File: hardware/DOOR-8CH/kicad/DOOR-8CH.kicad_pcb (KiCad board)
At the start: 4 copper layers, 260 x 160 mm, 230 parts, among them J1 FUSED_12V_CH1, J10 ACTUATOR_CH2, J11 ACTUATOR_CH3, J12 ACTUATOR_CH4, J13 ACTUATOR_CH5, J14 ACTUATOR_CH6, J15 ACTUATOR_CH7, J16 ACTUATOR_CH8, J2 FUSED_12V_CH2, J201 REED_A_OPEN_3V3_SIG_GND, J202 REED_A_CLOSED_3V3_SIG_GND, J203 REED_A_IN_PLACE_3V3_SIG_GND, J204 REED_B_OPEN_3V3_SIG_GND, J205 REED_B_CLOSED_3V3_SIG_GND, J206 REED_B_IN_PLACE_3V3_SIG_GND, J211 CAP_CS1_GND, J212 CAP_CS2_GND, J213 CAP_CS3_GND, J214 CAP_CS4_GND, J215 CAP_CS5_GND, J216 CAP_CS6_GND, J217 CAP_CS7_GND, J218 CAP_CS8_GND, J220 SWD_S1_3V3_DIO_CLK_NRST_GND, J230 LOGIC_12V_GND, J240 CANH_CANL_GND_SHIELD, J3 FUSED_12V_CH3, J4 FUSED_12V_CH4, J5 FUSED_12V_CH5, J6 FUSED_12V_CH6, J7 FUSED_12V_CH7, J8 FUSED_12V_CH8, J9 ACTUATOR_CH1, U1 VNH5019A-E, U2 VNH5019A-E, U230 AMS1117-3V3, U250 25LC256_SOIC8_CARRIER_ID, U3 VNH5019A-E, U4 VNH5019A-E, U5 VNH5019A-E, U6 VNH5019A-E, U7 VNH5019A-E, U8 VNH5019A-E

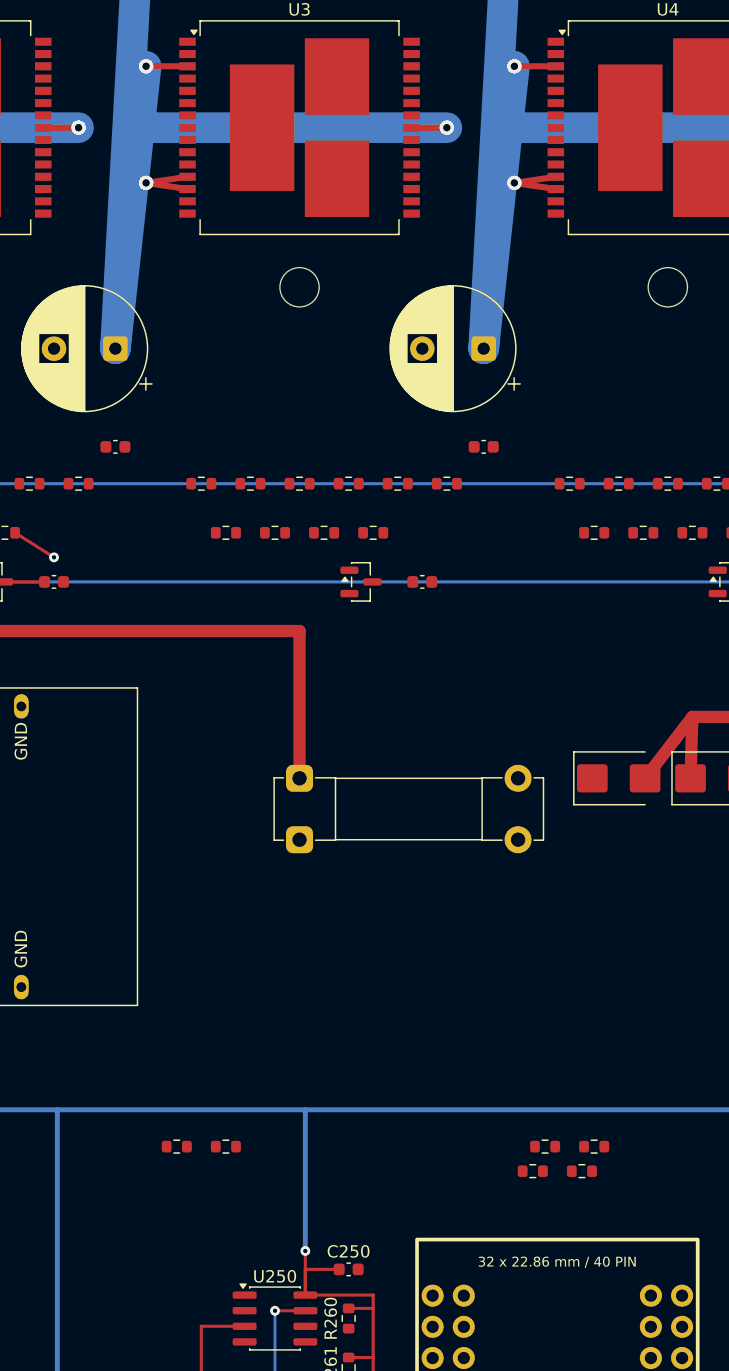
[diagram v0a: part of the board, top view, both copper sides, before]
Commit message: Route channel 3 controls and current measurement
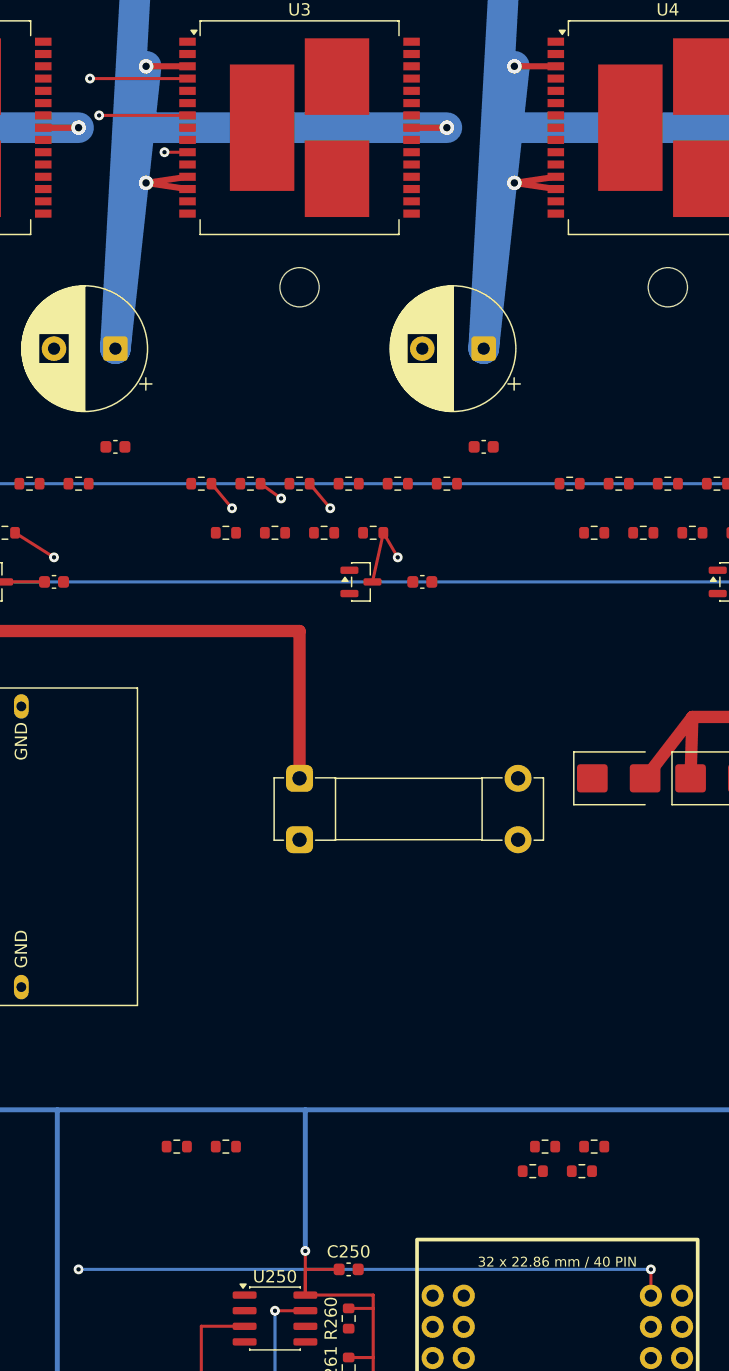
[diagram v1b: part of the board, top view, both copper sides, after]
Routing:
- net CH3_CURRENT_ADC: track 0.00 -> 139.2 mm, vias 0 -> 3
- net CH3_PWM: track 0.00 -> 72.6 mm, vias 0 -> 2
- net CH3_INA: track 0.00 -> 65.1 mm, vias 0 -> 2
- net CH3_INB: track 0.00 -> 41.6 mm, vias 0 -> 2
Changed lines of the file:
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@@
+	)
+	(segment
+		(start 82.5 65.2)
+		(end 80.83 64)
+		(width 0.25)
+		(layer "F.Cu")
+		(net "CH3_INB")
+	)
+	(segment
+		(start 74.88 37)
+		(end 73 37)
+		(width 0.25)
+		(layer "F.Cu")
+		(net "CH3_INB")
+	)
+	(via
+		(at 73 37)
+		(size 0.8)
+		(drill 0.35)
+		(layers "F.Cu" "B.Cu")
+		(net "CH3_INB")
+	)
+	(via
+		(at 82.5 65.2)
+		(size 0.8)
+		(drill 0.35)
+		(layers "F.Cu" "B.Cu")
+		(net "CH3_INB")
+	)
+	(segment
+		(start 73 37)
+		(end 73 65.2)
+		(width 0.25)
+		(layer "In2.Cu")
+		(net "CH3_INB")
+	)
+	(segment
+		(start 73 65.2)
+		(end 82.5 65.2)
+		(width 0.25)
+		(layer "In2.Cu")
+		(net "CH3_INB")
 	)
 	(segment
@@
 	)
 	(segment
+		(start 90.83 68)
+		(end 89.94 72)
+		(width 0.25)
+		(layer "F.Cu")
+		(net "CH3_CURRENT_ADC")
+	)
+	(segment
+		(start 90.83 68)
+		(end 92 70)
+		(width 0.25)
+		(layer "F.Cu")
+		(net "CH3_CURRENT_ADC")
+	)
+	(segment
+		(start 112.62 128)
+		(end 112.62 130.139999)
+		(width 0.25)
+		(layer "F.Cu")
+		(net "CH3_CURRENT_ADC")
+	)
+	(via
+		(at 92 70)
+		(size 0.8)
+		(drill 0.35)
+		(layers "F.Cu" "B.Cu")
+		(net "CH3_CURRENT_ADC")
+	)
+	(via
+		(at 112.62 128)
+		(size 0.8)
+		(drill 0.35)
+		(layers "F.Cu" "B.Cu")
+		(net "CH3_CURRENT_ADC")
+	)
+	(via
+		(at 66 128)
+		(size 0.8)
+		(drill 0.35)
+		(layers "F.Cu" "B.Cu")
+		(net "CH3_CURRENT_ADC")
+	)
+	(segment
+		(start 66 128)
+		(end 112.62 128)
+		(width 0.25)
+		(layer "B.Cu")
+		(net "CH3_CURRENT_ADC")
+	)
+	(segment
+		(start 92 70)
+		(end 92 105)
+		(width 0.25)
+		(layer "In1.Cu")
+		(net "CH3_CURRENT_ADC")
+	)
+	(segment
+		(start 66 105)
+		(end 66 128)
+		(width 0.25)
+		(layer "In1.Cu")
+		(net "CH3_CURRENT_ADC")
+	)
+	(segment
+		(start 92 105)
+		(end 66 105)
+		(width 0.25)
+		(layer "In1.Cu")
+		(net "CH3_CURRENT_ADC")
+	)
+	(segment
+		(start 78.5 66)
+		(end 76.83 64)
+		(width 0.25)
+		(layer "F.Cu")
+		(net "CH3_INA")
+	)
+	(segment
+		(start 74.88 31)
+		(end 66.93 31)
+		(width 0.25)
+		(layer "F.Cu")
+		(net "CH3_INA")
+	)
+	(via
+		(at 66.93 31)
+		(size 0.8)
+		(drill 0.35)
+		(layers "F.Cu" "B.Cu")
+		(net "CH3_INA")
+	)
+	(via
+		(at 78.5 66)
+		(size 0.8)
+		(drill 0.35)
+		(layers "F.Cu" "B.Cu")
+		(net "CH3_INA")
+	)
+	(segment
+		(start 66.93 70)
+		(end 78.5 70)
+		(width 0.25)
+		(layer "In2.Cu")
+		(net "CH3_INA")
+	)
+	(segment
+		(start 78.5 70)
+		(end 78.5 66)
+		(width 0.25)
+		(layer "In2.Cu")
+		(net "CH3_INA")
+	)
+	(segment
+		(start 66.93 31)
+		(end 66.93 70)
+		(width 0.25)
+		(layer "In2.Cu")
+		(net "CH3_INA")
+	)
+	(segment
+		(start 74.88 34)
+		(end 67.675 34)
+		(width 0.25)
+		(layer "F.Cu")
+		(net "CH3_PWM")
+	)
+	(segment
+		(start 86.5 66)
+		(end 84.83 64)
+		(width 0.25)
+		(layer "F.Cu")
+		(net "CH3_PWM")
+	)
+	(via
+		(at 86.5 66)
+		(size 0.8)
+		(drill 0.35)
+		(layers "F.Cu" "B.Cu")
+		(net "CH3_PWM")
+	)
+	(via
+		(at 67.675 34)
+		(size 0.8)
+		(drill 0.35)
+		(layers "F.Cu" "B.Cu")
+		(net "CH3_PWM")
+	)
+	(segment
+		(start 67.675 72)
+		(end 86.5 72)
+		(width 0.25)
+		(layer "In1.Cu")
+		(net "CH3_PWM")
+	)
+	(segment
+		(start 67.675 34)
+		(end 67.675 72)
+		(width 0.25)
+		(layer "In1.Cu")
+		(net "CH3_PWM")
+	)
+	(segment
+		(start 86.5 72)
+		(end 86.5 66)
+		(width 0.25)
+		(layer "In1.Cu")
+		(net "CH3_PWM")
+	)
+	(segment

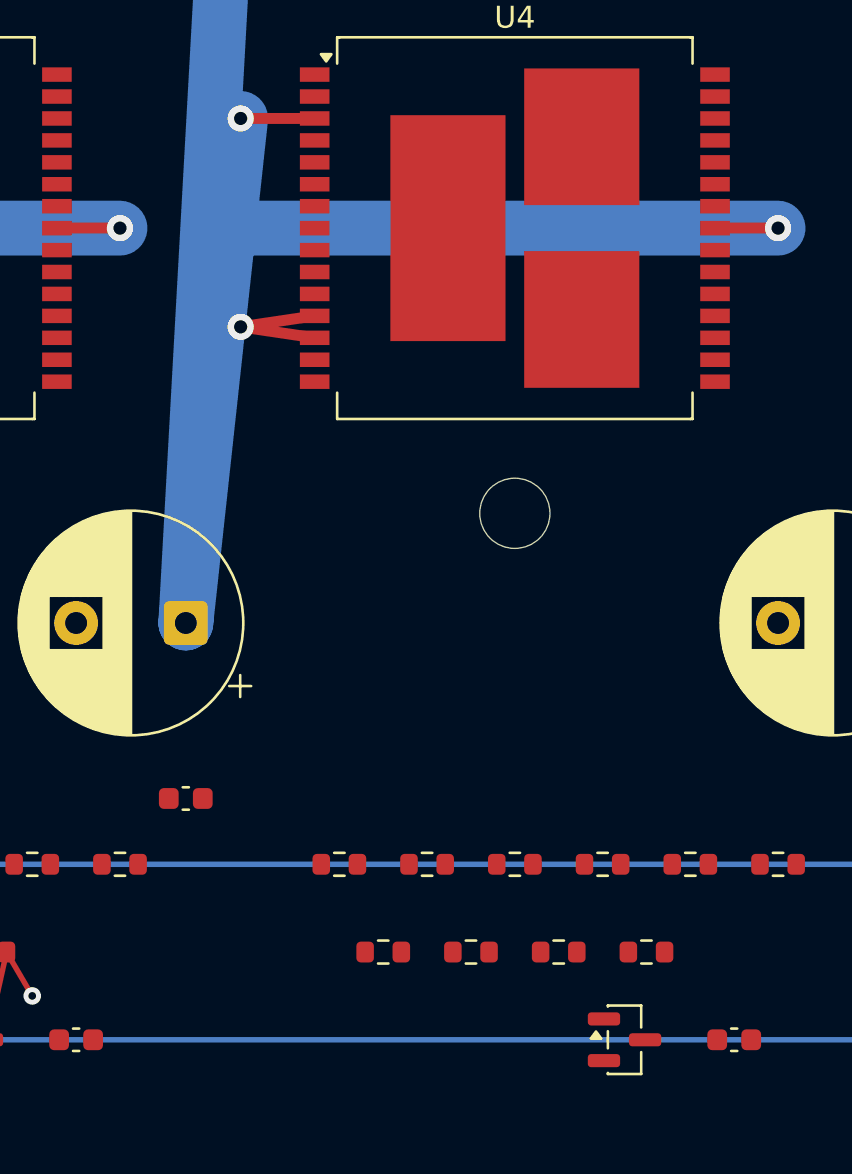
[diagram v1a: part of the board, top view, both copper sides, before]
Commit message: Route channel 4 controls and local current filter
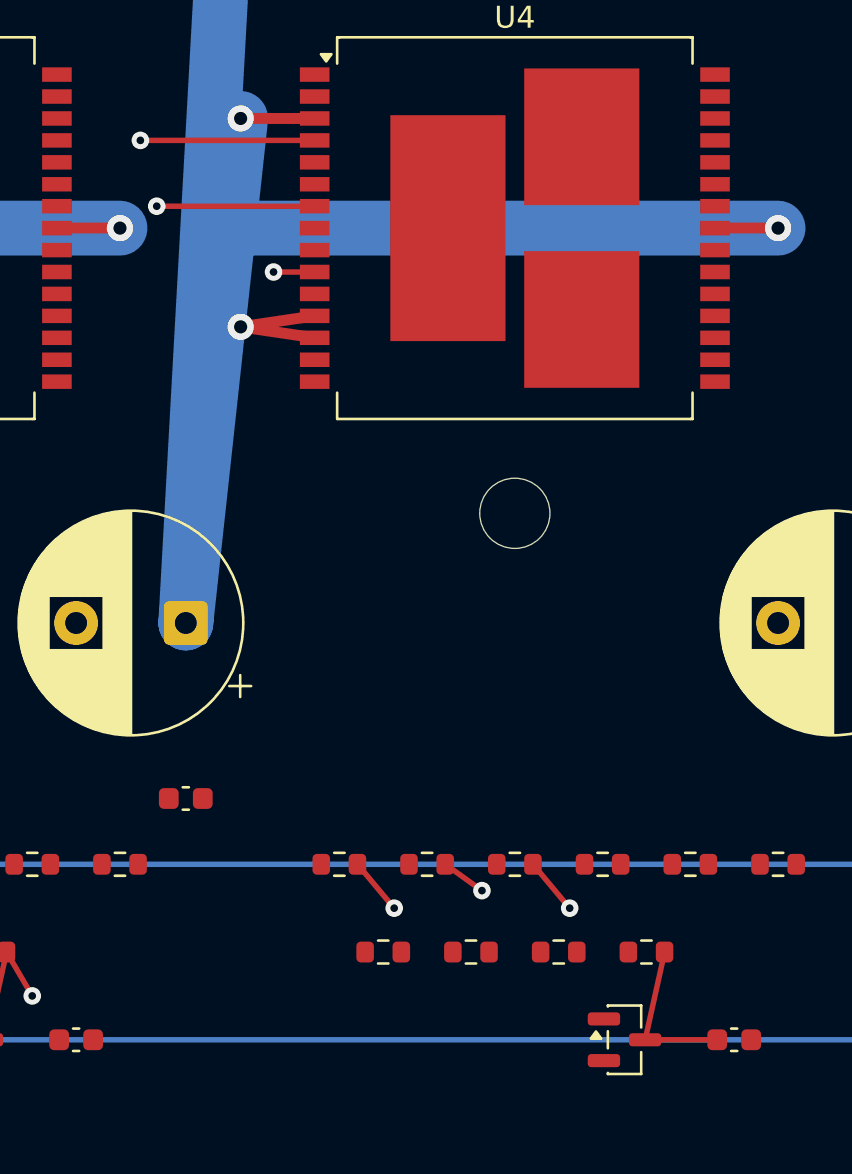
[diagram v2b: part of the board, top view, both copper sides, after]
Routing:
- net CH4_PWM: track 0.00 -> 72.6 mm, vias 0 -> 2
- net CH4_INA: track 0.00 -> 65.1 mm, vias 0 -> 2
- net CH4_INB: track 0.00 -> 41.6 mm, vias 0 -> 2
- net CH4_CURRENT_ADC: track 0.00 -> 7.39 mm
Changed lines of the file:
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@@
+	)
+	(segment
+		(start 120.83 68)
+		(end 119.94 72)
+		(width 0.25)
+		(layer "F.Cu")
+		(net "CH4_CURRENT_ADC")
+	)
+	(segment
+		(start 119.94 72)
+		(end 123.23 72)
+		(width 0.25)
+		(layer "F.Cu")
+		(net "CH4_CURRENT_ADC")
 	)
 	(segment
@@
 	)
 	(segment
+		(start 104.88 37)
+		(end 103 37)
+		(width 0.25)
+		(layer "F.Cu")
+		(net "CH4_INB")
+	)
+	(segment
+		(start 112.5 65.2)
+		(end 110.83 64)
+		(width 0.25)
+		(layer "F.Cu")
+		(net "CH4_INB")
+	)
+	(via
+		(at 112.5 65.2)
+		(size 0.8)
+		(drill 0.35)
+		(layers "F.Cu" "B.Cu")
+		(net "CH4_INB")
+	)
+	(via
+		(at 103 37)
+		(size 0.8)
+		(drill 0.35)
+		(layers "F.Cu" "B.Cu")
+		(net "CH4_INB")
+	)
+	(segment
+		(start 103 37)
+		(end 103 65.2)
+		(width 0.25)
+		(layer "In2.Cu")
+		(net "CH4_INB")
+	)
+	(segment
+		(start 103 65.2)
+		(end 112.5 65.2)
+		(width 0.25)
+		(layer "In2.Cu")
+		(net "CH4_INB")
+	)
+	(segment
 		(start 55.18 68)
 		(end 55.18 69)
@@
 	)
 	(segment
+		(start 116.5 66)
+		(end 114.83 64)
+		(width 0.25)
+		(layer "F.Cu")
+		(net "CH4_PWM")
+	)
+	(segment
+		(start 104.88 34)
+		(end 97.675 34)
+		(width 0.25)
+		(layer "F.Cu")
+		(net "CH4_PWM")
+	)
+	(via
+		(at 97.675 34)
+		(size 0.8)
+		(drill 0.35)
+		(layers "F.Cu" "B.Cu")
+		(net "CH4_PWM")
+	)
+	(via
+		(at 116.5 66)
+		(size 0.8)
+		(drill 0.35)
+		(layers "F.Cu" "B.Cu")
+		(net "CH4_PWM")
+	)
+	(segment
+		(start 97.675 34)
+		(end 97.675 72)
+		(width 0.25)
+		(layer "In1.Cu")
+		(net "CH4_PWM")
+	)
+	(segment
+		(start 97.675 72)
+		(end 116.5 72)
+		(width 0.25)
+		(layer "In1.Cu")
+		(net "CH4_PWM")
+	)
+	(segment
+		(start 116.5 72)
+		(end 116.5 66)
+		(width 0.25)
+		(layer "In1.Cu")
+		(net "CH4_PWM")
+	)
+	(segment
+		(start 104.88 31)
+		(end 96.93 31)
+		(width 0.25)
+		(layer "F.Cu")
+		(net "CH4_INA")
+	)
+	(segment
+		(start 108.5 66)
+		(end 106.83 64)
+		(width 0.25)
+		(layer "F.Cu")
+		(net "CH4_INA")
+	)
+	(via
+		(at 96.93 31)
+		(size 0.8)
+		(drill 0.35)
+		(layers "F.Cu" "B.Cu")
+		(net "CH4_INA")
+	)
+	(via
+		(at 108.5 66)
+		(size 0.8)
+		(drill 0.35)
+		(layers "F.Cu" "B.Cu")
+		(net "CH4_INA")
+	)
+	(segment
+		(start 96.93 70)
+		(end 108.5 70)
+		(width 0.25)
+		(layer "In2.Cu")
+		(net "CH4_INA")
+	)
+	(segment
+		(start 108.5 70)
+		(end 108.5 66)
+		(width 0.25)
+		(layer "In2.Cu")
+		(net "CH4_INA")
+	)
+	(segment
+		(start 96.93 31)
+		(end 96.93 70)
+		(width 0.25)
+		(layer "In2.Cu")
+		(net "CH4_INA")
+	)
+	(segment

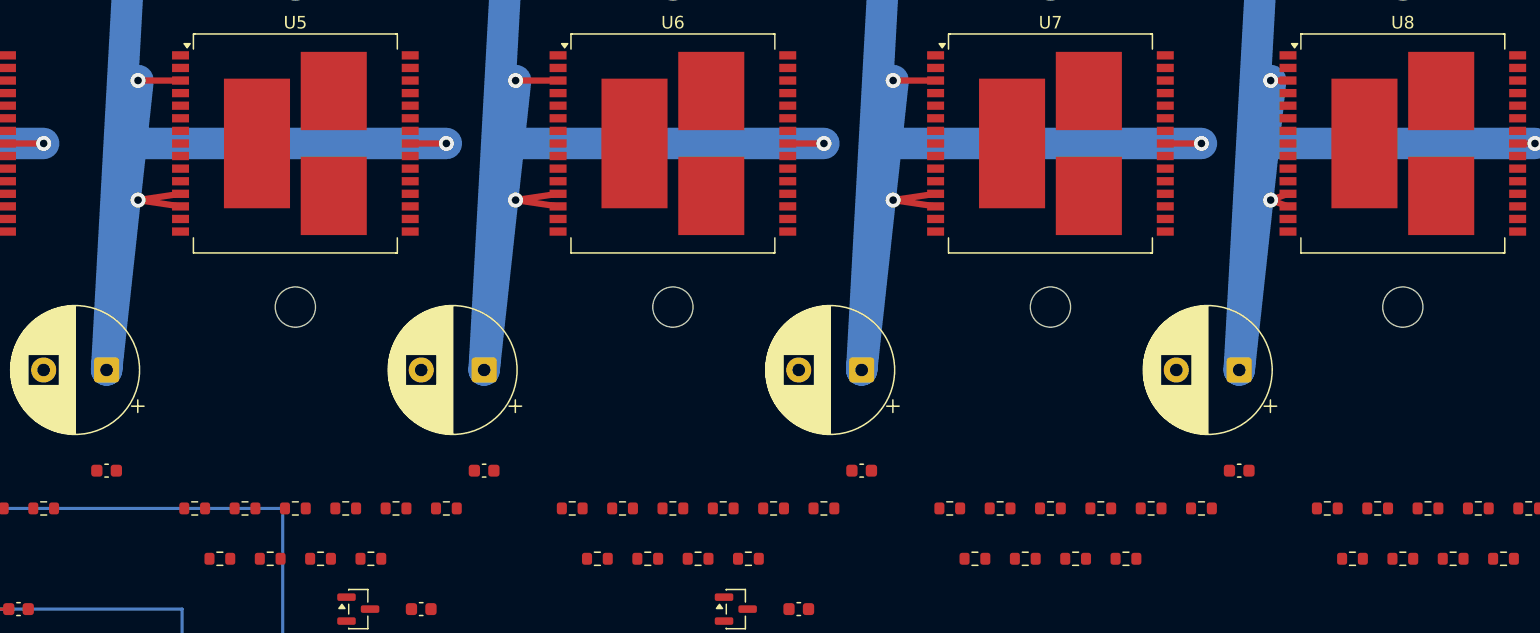
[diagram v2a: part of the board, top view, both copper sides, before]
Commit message: Route channels 5-8 VNH control inputs
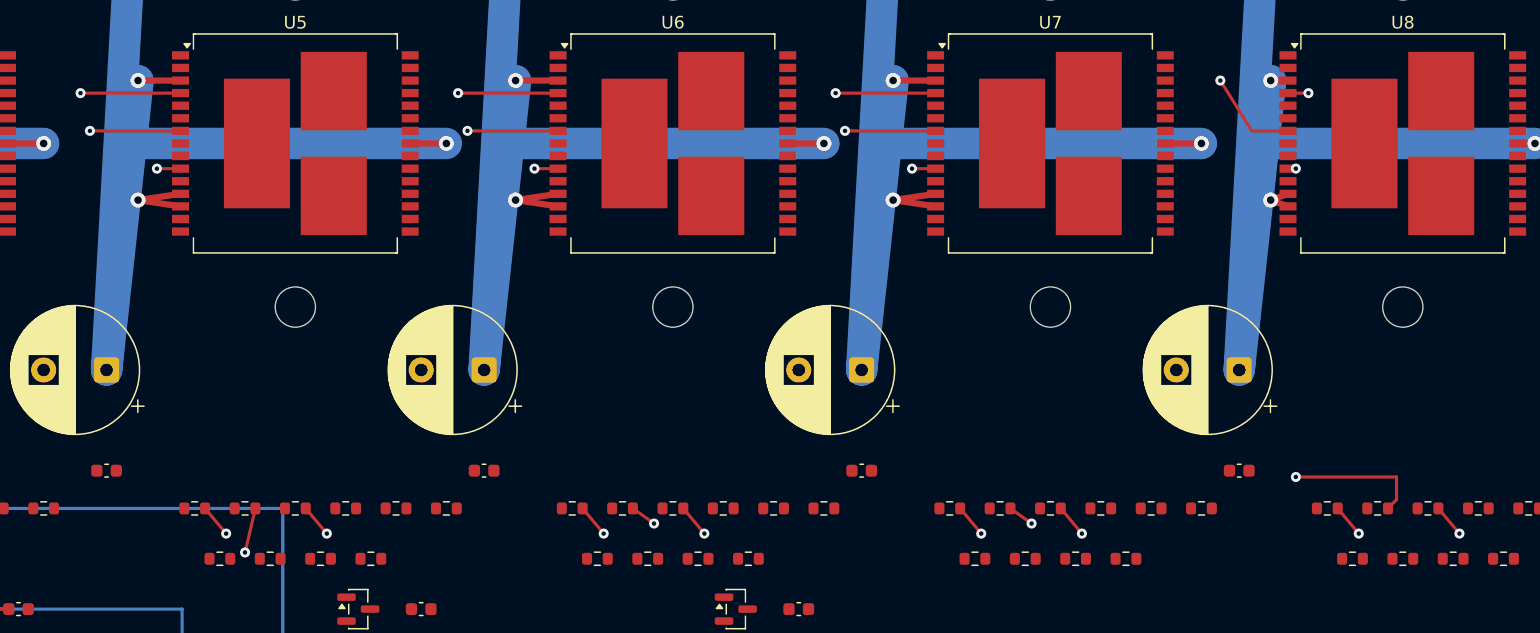
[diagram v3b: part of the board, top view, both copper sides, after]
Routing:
- net CH8_PWM: track 0.00 -> 88.2 mm, vias 0 -> 2
- net CH7_PWM: track 0.00 -> 72.6 mm, vias 0 -> 2
- net CH6_PWM: track 0.00 -> 72.6 mm, vias 0 -> 2
- net CH5_PWM: track 0.00 -> 72.6 mm, vias 0 -> 2
- net CH7_INA: track 0.00 -> 65.1 mm, vias 0 -> 2
- net CH6_INA: track 0.00 -> 65.1 mm, vias 0 -> 2
- net CH5_INA: track 0.00 -> 65.1 mm, vias 0 -> 2
- net CH8_INA: track 0.00 -> 51.2 mm, vias 0 -> 2
- net CH5_INB: track 0.00 -> 43.0 mm, vias 0 -> 2
- net CH7_INB: track 0.00 -> 41.6 mm, vias 0 -> 2
- net CH6_INB: track 0.00 -> 41.6 mm, vias 0 -> 2
- net CH8_INB: track 0.00 -> 35.9 mm, vias 0 -> 2

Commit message: Route channels 5-8 current filters
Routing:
- net CH7_CURRENT_ADC: track 0.00 -> 26.7 mm
- net CH8_CURRENT_ADC: track 0.00 -> 11.3 mm
- net CH6_CURRENT_ADC: track 0.00 -> 7.38 mm
- net CH5_CURRENT_ADC: track 0.00 -> 7.38 mm
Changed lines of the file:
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@@
+	)
+	(segment
+		(start 242.825 68)
+		(end 240.9375 76)
+		(width 0.25)
+		(layer "F.Cu")
+		(net "CH8_CURRENT_ADC")
+	)
+	(segment
+		(start 240.9375 76)
+		(end 243.225 78)
+		(width 0.25)
+		(layer "F.Cu")
+		(net "CH8_CURRENT_ADC")
 	)
 	(segment
@@
 		(layer "In1.Cu")
 		(net "CH7_PWM")
+	)
+	(segment
+		(start 212 84)
+		(end 205.5 84)
+		(width 0.25)
+		(layer "F.Cu")
+		(net "CH7_CURRENT_ADC")
+	)
+	(segment
+		(start 212 80)
+		(end 212 84)
+		(width 0.25)
+		(layer "F.Cu")
+		(net "CH7_CURRENT_ADC")
+	)
+	(segment
+		(start 210.9375 78)
+		(end 212 80)
+		(width 0.25)
+		(layer "F.Cu")
+		(net "CH7_CURRENT_ADC")
+	)
+	(segment
+		(start 205.5 82)
+		(end 207.225 82)
+		(width 0.25)
+		(layer "F.Cu")
+		(net "CH7_CURRENT_ADC")
+	)
+	(segment
+		(start 212.825 68)
+		(end 210.9375 78)
+		(width 0.25)
+		(layer "F.Cu")
+		(net "CH7_CURRENT_ADC")
+	)
+	(segment
+		(start 205.5 84)
+		(end 205.5 82)
+		(width 0.25)
+		(layer "F.Cu")
+		(net "CH7_CURRENT_ADC")
 	)
 	(segment
@@
 	)
 	(segment
+		(start 151.9375 72)
+		(end 155.225 72)
+		(width 0.25)
+		(layer "F.Cu")
+		(net "CH5_CURRENT_ADC")
+	)
+	(segment
+		(start 152.825 68)
+		(end 151.9375 72)
+		(width 0.25)
+		(layer "F.Cu")
+		(net "CH5_CURRENT_ADC")
+	)
+	(segment
 		(start 230.5 66)
 		(end 228.825 64)
@@
 	)
 	(segment
+		(start 182.825 68)
+		(end 181.9375 72)
+		(width 0.25)
+		(layer "F.Cu")
+		(net "CH6_CURRENT_ADC")
+	)
+	(segment
+		(start 181.9375 72)
+		(end 185.225 72)
+		(width 0.25)
+		(layer "F.Cu")
+		(net "CH6_CURRENT_ADC")
+	)
+	(segment
